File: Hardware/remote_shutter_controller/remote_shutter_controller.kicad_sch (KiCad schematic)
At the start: 14 parts

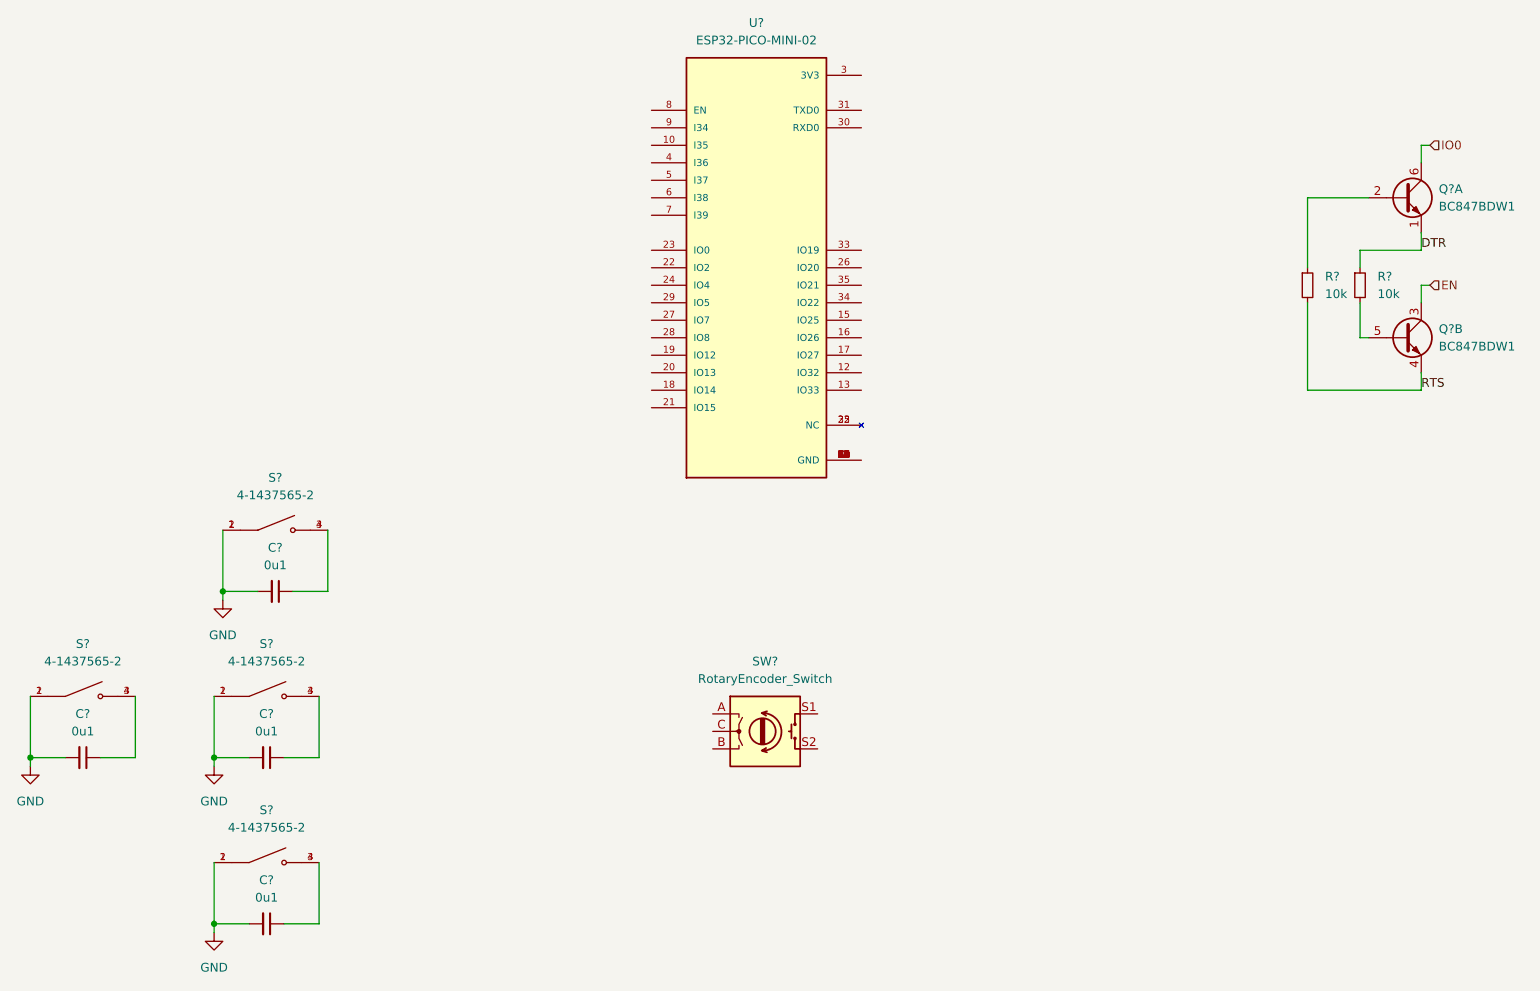
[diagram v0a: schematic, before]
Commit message: Work on the controller PCB
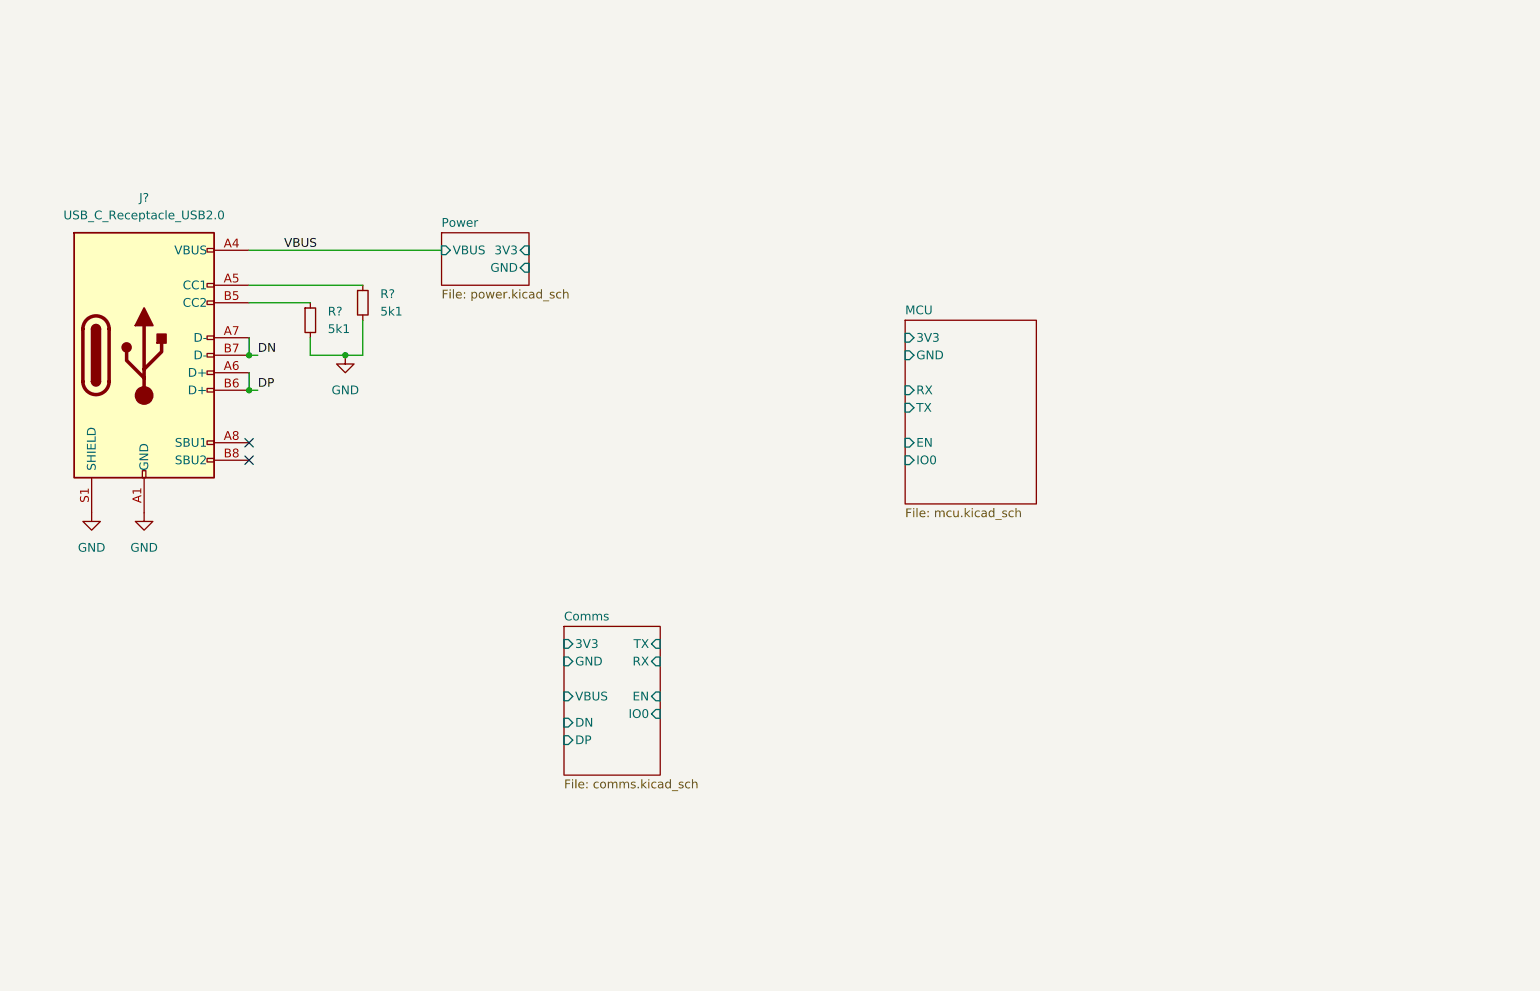
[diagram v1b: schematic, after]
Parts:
- removed C? (x4): 0u1, symbol Device:C_Small
- removed Q? (x2): BC847BDW1, Package_TO_SOT_SMD:SOT-363_SC-70-6, symbol Transistor_BJT:BC847BDW1
- removed R? (x2): 10k, Resistor_SMD:R_0603_1608Metric_Pad0.98x0.95mm_HandSolder, symbol Device:R_Small
- removed S? (x4): 4-1437565-2, footprint:SW_4-1437565-2, symbol 4-1437565-2:4-1437565-2
- removed SW?: RotaryEncoder_Switch, symbol Device:RotaryEncoder_Switch
- removed U?: ESP32-PICO-MINI-02, MODULE_ESP32-PICO-MINI-02, symbol ESP32-PICO-MINI-02:ESP32-PICO-MINI-02
- added J?: USB_C_Receptacle_USB2.0, Connector_USB:USB_C_Receptacle_XKB_U262-16XN-4BVC11, symbol Connector:USB_C_Receptacle_USB2.0
- added R? (x2): 5k1, Resistor_SMD:R_0603_1608Metric_Pad0.98x0.95mm_HandSolder, symbol Device:R_Small
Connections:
- net GND: now also J?.A1 (GND), J?.A12 (GND), J?.B1 (GND), J?.B12 (GND), J?.S1 (SHIELD), R?.2, R?.2
- new net: J?.A5 (CC1), R?.1
- new net: J?.B5 (CC2), R?.1
- new net DN: J?.A7 (D-), J?.B7 (D-)
- new net DP: J?.A6 (D+), J?.B6 (D+)
- new net VBUS: J?.A4 (VBUS), J?.A9 (VBUS), J?.B4 (VBUS), J?.B9 (VBUS)
- no-connect marks 0 -> 2
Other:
- added sheet Comms (comms.kicad_sch)
- added sheet MCU (mcu.kicad_sch)
- added sheet Power (power.kicad_sch)

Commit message: Schematic updates. First export to PCB
Added 9V line, OLED switch circuit. Added OLED footprint.
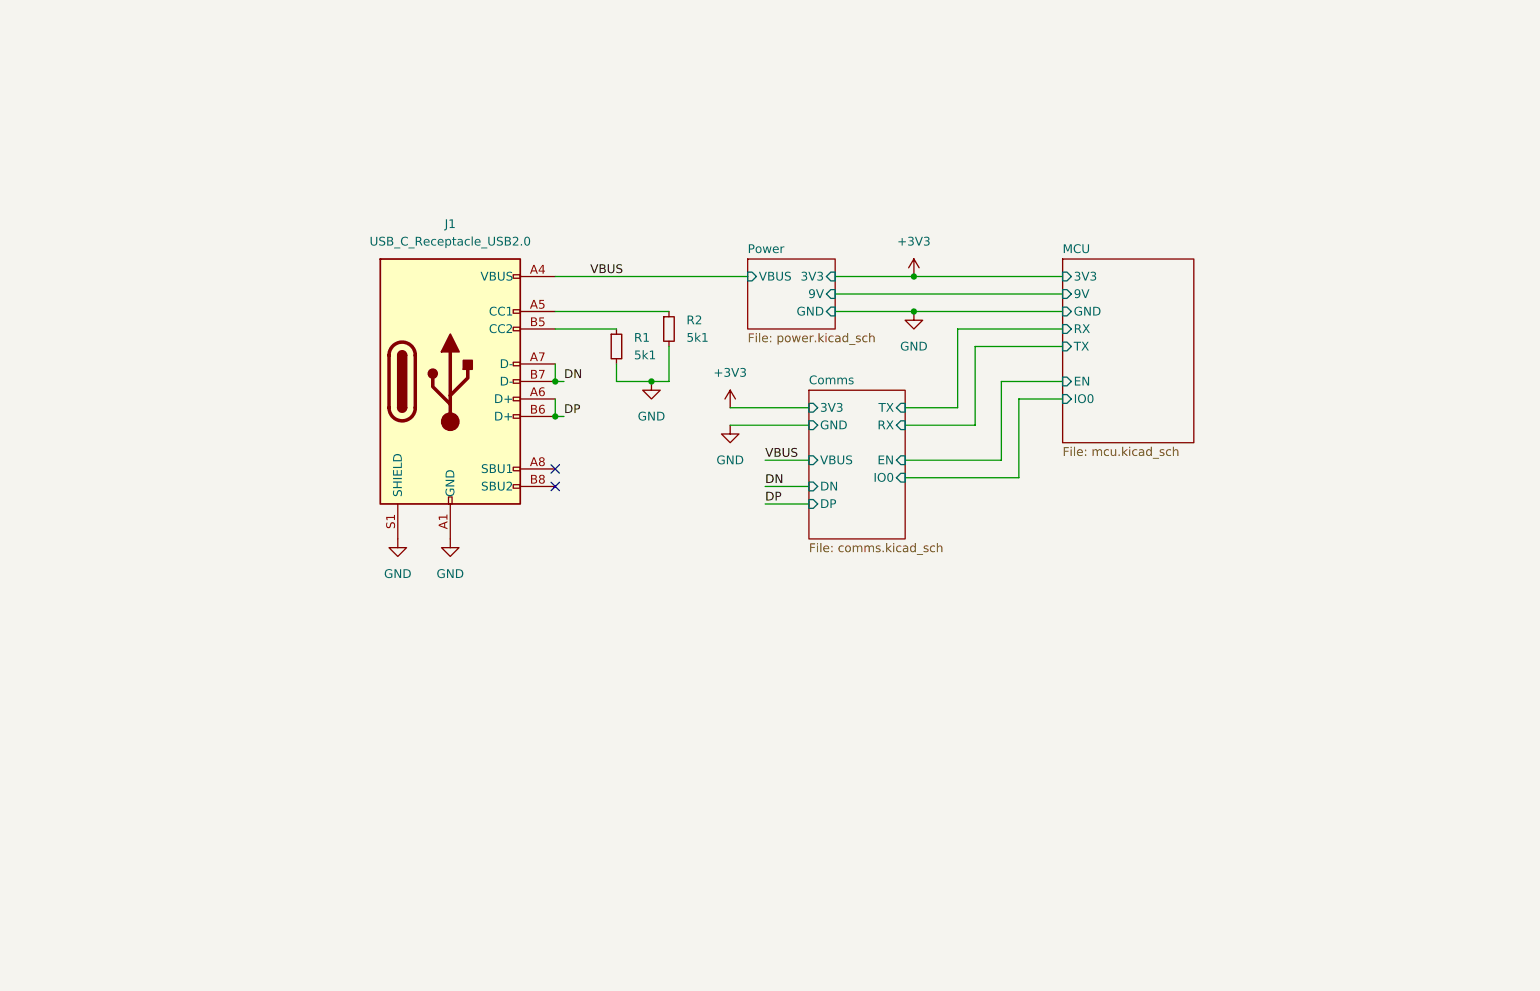
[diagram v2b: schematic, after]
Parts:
- gave numbers to parts that had none: 3
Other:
- sheet MCU ports: added 9V; removed none
- sheet Power ports: added 9V; removed none
- moved on the sheet: J1, R1, R2
